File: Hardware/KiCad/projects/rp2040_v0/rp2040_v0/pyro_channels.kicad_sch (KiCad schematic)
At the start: 30 parts, among them J24 Screw_Terminal_01x02, J25 Screw_Terminal_01x02, J26 Screw_Terminal_01x02, J27 Screw_Terminal_01x02, J28 Screw_Terminal_01x02, Q2 AO3400A, Q3 AO3400A, Q4 AO3400A, Q5 AO3400A

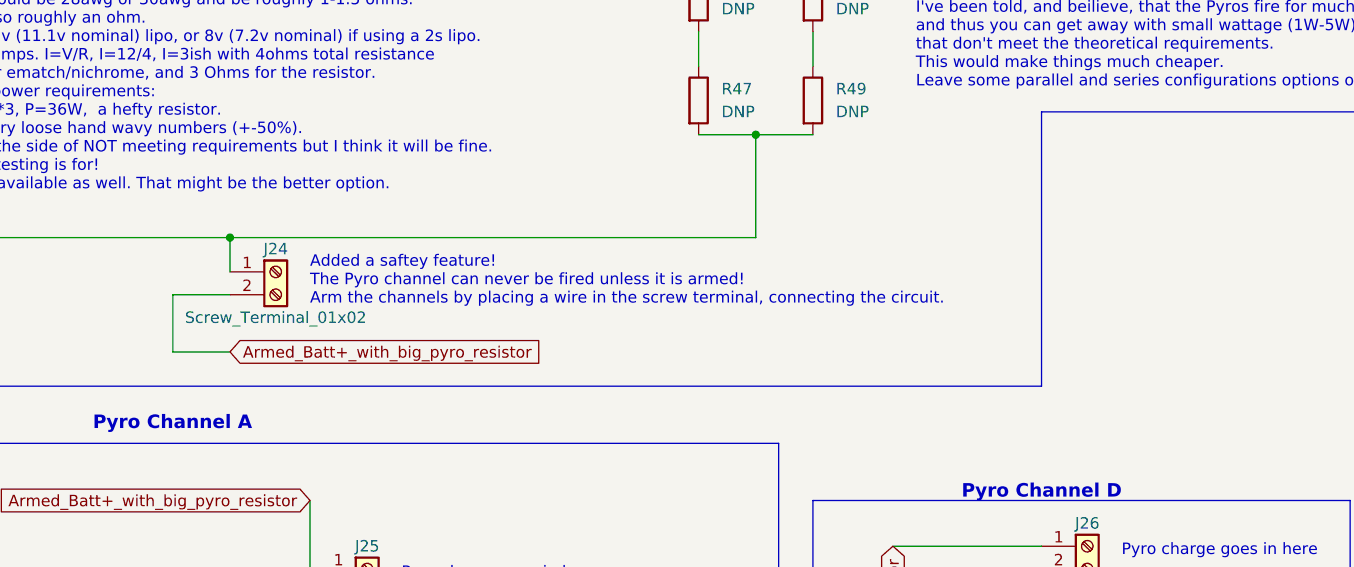
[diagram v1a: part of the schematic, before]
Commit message: Change arming screw terminal to jumper
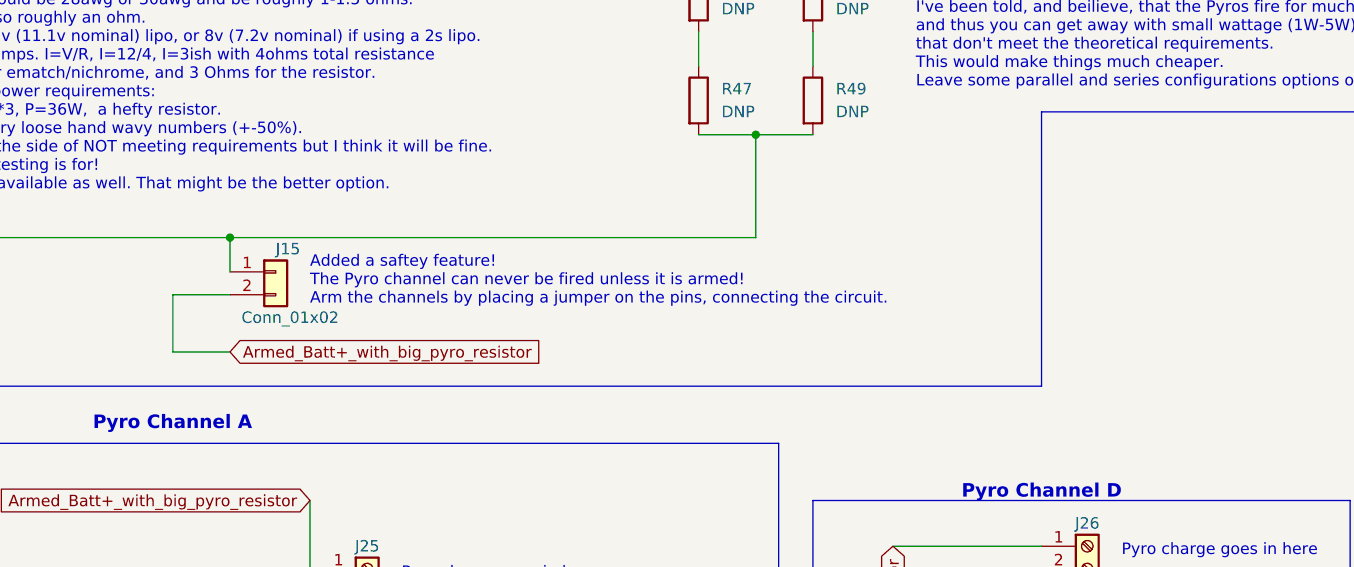
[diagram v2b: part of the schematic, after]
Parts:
- removed J24: Screw_Terminal_01x02, easyeda2kicad:CONN-TH_XY301V-A-5.0-2P, symbol Connector:Screw_Terminal_01x02
- added J15: Conn_01x02, Connector_PinHeader_2.54mm:PinHeader_1x02_P2.54mm_Vertical, symbol Connector_Generic:Conn_01x02
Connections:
- net Armed_Batt+_with_big_pyro_resistor: now also J15.2 (Pin_2)
- net at R39.2, R47.2, R49.2: now also J15.1 (Pin_1)
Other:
- note added: "Added a saftey feature! The Pyro channel can never be fired unless it is armed! Arm the channels by placing a jumper on the pins, connecting the circuit."
- note removed: "Added a saftey feature! The Pyro channel can never be fired unless it is armed! Arm the channels by placing a wire in the screw terminal, connecting the circuit."
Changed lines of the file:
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@@
     (effects (font (size 1.27 1.27)) (justify left bottom))
   )
-  (text "Added a saftey feature!\nThe Pyro channel can never be fired unless it is armed!\nArm the channels by placing a wire in the screw terminal, connecting the circuit."
+  (text "Added a saftey feature!\nThe Pyro channel can never be fired unless it is armed!\nArm the channels by placing a jumper on the pins, connecting the circuit."
     (at 83.82 76.2 0)
     (effects (font (size 1.27 1.27)) (justify left bottom))
@@
     (pin "1")
   )
+  (symbol (lib_id "Connector_Generic:Conn_01x02") (at 80.01 72.39 0) (unit 1)
+    (in_bom yes) (on_board yes)
+    (property "Reference" "J15" (id 0) (at 80.01 69.85 0)
+      (effects (font (size 1.27 1.27)) (justify left))
+    )
+    (property "Value" "Conn_01x02" (id 1) (at 76.2 77.47 0)
+      (effects (font (size 1.27 1.27)) (justify left))
+    )
+    (property "Footprint" "Connector_PinHeader_2.54mm:PinHeader_1x02_P2.54mm_Vertical" (id 2) (at 80.01 72.39 0)
+      (effects (font (size 1.27 1.27)) hide)
+    )
+    (property "Datasheet" "~" (id 3) (at 80.01 72.39 0)
+      (effects (font (size 1.27 1.27)) hide)
+    )
+    (pin "1")
+    (pin "2")
+  )
   (symbol (lib_id "Device:R_Small") (at 238.76 91.44 180) (unit 1)
     (in_bom yes) (on_board yes) (fields_autoplaced)
@@
     (pin "1")
   )
-  (symbol (lib_id "Connector:Screw_Terminal_01x02") (at 80.01 72.39 0) (unit 1)
-    (in_bom yes) (on_board yes)
-    (property "Reference" "J24" (id 0) (at 80.01 69.85 0))
-    (property "Value" "Screw_Terminal_01x02" (id 1) (at 80.01 77.47 0))
-    (property "Footprint" "easyeda2kicad:CONN-TH_XY301V-A-5.0-2P" (id 2) (at 80.01 72.39 0)
-      (effects (font (size 1.27 1.27)) hide)
-    )
-    (property "Datasheet" "~" (id 3) (at 80.01 72.39 0)
-      (effects (font (size 1.27 1.27)) hide)
-    )
-    (pin "1")
-    (pin "2")
-  )
   (symbol (lib_id "power:GND") (at 97.79 140.97 0) (unit 1)

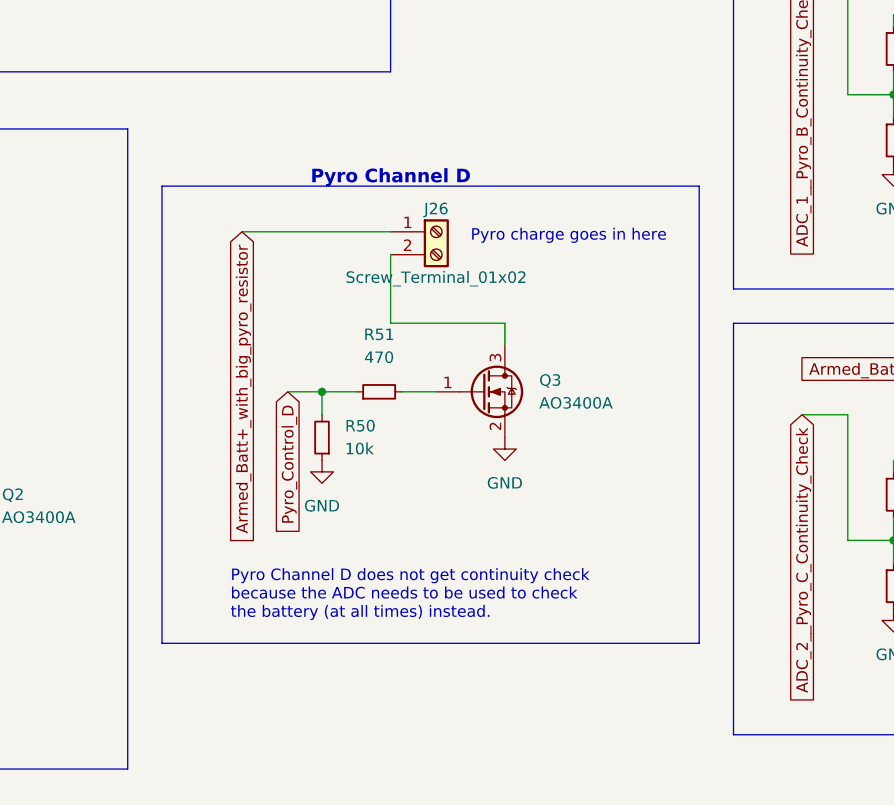
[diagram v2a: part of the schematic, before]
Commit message: Remove pyro channel D
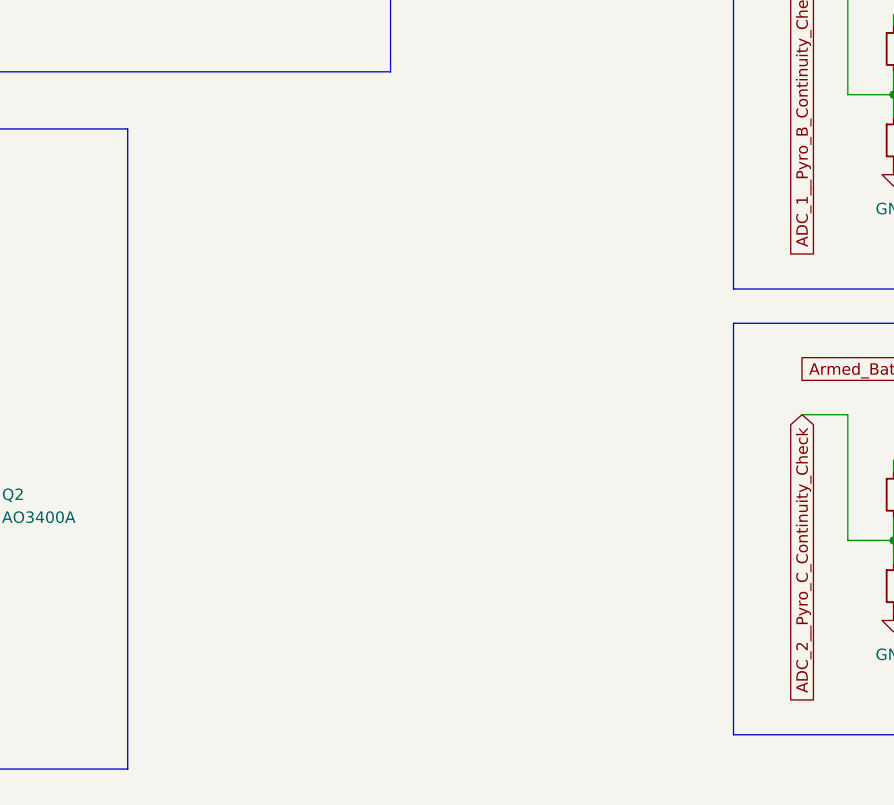
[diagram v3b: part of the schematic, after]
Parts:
- removed J26: Screw_Terminal_01x02, easyeda2kicad:CONN-TH_XY301V-A-5.0-2P, symbol Connector:Screw_Terminal_01x02
- removed Q3: AO3400A, Package_TO_SOT_SMD:SOT-23, symbol Transistor_FET:AO3400A
- removed R50: 10k, Resistor_SMD:R_0402_1005Metric, symbol Device:R_Small
- removed R51: 470, Resistor_SMD:R_0402_1005Metric, symbol Device:R_Small
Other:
- note removed: "Pyro Channel D"
- note removed: "Pyro Channel D does not get continuity check because the ADC needs to be used to check the battery (at all times) instead."
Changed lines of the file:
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@@
   (junction (at 246.38 78.74) (diameter 0) (color 0 0 0 0)
   )
-  (junction (at 157.48 120.65) (diameter 0) (color 0 0 0 0)
-  )
   (junction (at 31.75 27.94) (diameter 0) (color 0 0 0 0)
   )
@@
     (stroke (width 0) (type default) (color 0 0 0 0))
   )
-  (wire (pts (xy 177.8 115.57) (xy 177.8 113.03))
-    (stroke (width 0) (type default) (color 0 0 0 0))
-  )
   (wire (pts (xy 220.98 78.74) (xy 246.38 78.74))
     (stroke (width 0) (type default) (color 0 0 0 0))
@@
     (stroke (width 0) (type default) (color 0 0 0 0))
   )
-  (wire (pts (xy 157.48 120.65) (xy 161.29 120.65))
-    (stroke (width 0) (type default) (color 0 0 0 0))
-  )
   (wire (pts (xy 259.08 78.74) (xy 246.38 78.74))
     (stroke (width 0) (type default) (color 0 0 0 0))
@@
     (stroke (width 0) (type default) (color 0 0 0 0))
   )
-  (wire (pts (xy 165.1 105.41) (xy 165.1 113.03))
-    (stroke (width 0) (type default) (color 0 0 0 0))
-  )
   (wire (pts (xy 55.88 173.99) (xy 55.88 180.34))
     (stroke (width 0) (type default) (color 0 0 0 0))
@@
     (stroke (width 0) (type default) (color 0 0 0 0))
   )
-  (wire (pts (xy 177.8 113.03) (xy 165.1 113.03))
-    (stroke (width 0) (type default) (color 0 0 0 0))
-  )
   (polyline (pts (xy 203.2 158.75) (xy 284.48 158.75))
     (stroke (width 0) (type default) (color 0 0 0 0))
@@
     (stroke (width 0) (type default) (color 0 0 0 0))
   )
-  (wire (pts (xy 148.59 102.87) (xy 165.1 102.87))
-    (stroke (width 0) (type default) (color 0 0 0 0))
-  )
   (wire (pts (xy 127 57.15) (xy 133.35 57.15))
     (stroke (width 0) (type default) (color 0 0 0 0))
@@
     (stroke (width 0) (type default) (color 0 0 0 0))
   )
-  (wire (pts (xy 157.48 120.65) (xy 157.48 123.19))
-    (stroke (width 0) (type default) (color 0 0 0 0))
-  )
   (wire (pts (xy 215.9 137.16) (xy 220.98 137.16))
     (stroke (width 0) (type default) (color 0 0 0 0))
@@
     (stroke (width 0) (type default) (color 0 0 0 0))
   )
-  (polyline (pts (xy 199.39 97.79) (xy 139.7 97.79))
-    (stroke (width 0) (type default) (color 0 0 0 0))
-  )
   (wire (pts (xy 97.79 133.35) (xy 101.6 133.35))
     (stroke (width 0) (type default) (color 0 0 0 0))
@@
     (stroke (width 0) (type default) (color 0 0 0 0))
   )
-  (polyline (pts (xy 139.7 148.59) (xy 199.39 148.59))
-    (stroke (width 0) (type default) (color 0 0 0 0))
-  )
   (wire (pts (xy 133.35 57.15) (xy 133.35 68.58))
     (stroke (width 0) (type default) (color 0 0 0 0))
@@
     (stroke (width 0) (type default) (color 0 0 0 0))
   )
-  (wire (pts (xy 153.67 120.65) (xy 157.48 120.65))
-    (stroke (width 0) (type default) (color 0 0 0 0))
-  )
   (polyline (pts (xy 135.89 91.44) (xy 15.24 91.44))
     (stroke (width 0) (type default) (color 0 0 0 0))
@@
     (stroke (width 0) (type default) (color 0 0 0 0))
   )
-  (polyline (pts (xy 139.7 97.79) (xy 139.7 148.59))
-    (stroke (width 0) (type default) (color 0 0 0 0))
-  )
   (polyline (pts (xy 165.1 54.61) (xy 231.14 54.61))
     (stroke (width 0) (type default) (color 0 0 0 0))
@@
     (stroke (width 0) (type default) (color 0 0 0 0))
   )
-  (polyline (pts (xy 199.39 97.79) (xy 199.39 148.59))
-    (stroke (width 0) (type default) (color 0 0 0 0))
-  )
   (polyline (pts (xy 15.24 162.56) (xy 135.89 162.56))
     (stroke (width 0) (type default) (color 0 0 0 0))
@@
   )
   (wire (pts (xy 259.08 128.27) (xy 246.38 128.27))
-    (stroke (width 0) (type default) (color 0 0 0 0))
-  )
-  (wire (pts (xy 166.37 120.65) (xy 170.18 120.65))
     (stroke (width 0) (type default) (color 0 0 0 0))
   )
@@
     (effects (font (size 1.27 1.27)) (justify left bottom))
   )
-  (text "Pyro Channel D" (at 156.21 97.79 0)
-    (effects (font (size 1.5 1.5) (thickness 0.3) bold) (justify left bottom))
-  )
   (text "Inrush current\nprotection resistor" (at 95.25 125.73 0)
     (effects (font (size 1.27 1.27)) (justify left bottom))
@@
     (effects (font (size 1.5 1.5) (thickness 0.3) bold) (justify left bottom))
   )
-  (text "Pyro Channel D does not get continuity check\nbecause the ADC needs to be used to check\nthe battery (at all times) instead."
-    (at 147.32 146.05 0)
-    (effects (font (size 1.27 1.27)) (justify left bottom))
-  )
-  (text "Pyro charge goes in here" (at 173.99 104.14 0)
-    (effects (font (size 1.27 1.27)) (justify left bottom))
-  )
   (text "Pyro power source with resistor\n" (at 107.95 15.24 0)
     (effects (font (size 1.5 1.5) (thickness 0.3) bold) (justify left bottom))
@@
     )
   )
-  (global_label "Pyro_Control_D" (shape input) (at 153.67 120.65 270) (fields_autoplaced)
-    (effects (font (size 1.27 1.27)) (justify right))
-    (property "Intersheet References" "${INTERSHEET_REFS}" (id 0) (at 153.5906 129.4131 90)
-      (effects (font (size 1.27 1.27)) (justify right) hide)
-    )
-  )
   (global_label "ADC_1__Pyro_B_Continuity_Check" (shape input) (at 210.82 73.66 270) (fields_autoplaced)
     (effects (font (size 1.27 1.27)) (justify right))
@@
     (effects (font (size 1.27 1.27)) (justify right))
     (property "Intersheet References" "${INTERSHEET_REFS}" (id 0) (at 215.4221 118.1894 0)
-      (effects (font (size 1.27 1.27)) (justify right) hide)
-    )
-  )
-  (global_label "Armed_Batt+_with_big_pyro_resistor" (shape input) (at 148.59 102.87 270) (fields_autoplaced)
-    (effects (font (size 1.27 1.27)) (justify right))
-    (property "Intersheet References" "${INTERSHEET_REFS}" (id 0) (at 148.6694 132.5579 90)
       (effects (font (size 1.27 1.27)) (justify right) hide)
     )
@@
     )
   )
-  (symbol (lib_id "Device:R_Small") (at 163.83 120.65 90) (unit 1)
-    (in_bom yes) (on_board yes) (fields_autoplaced)
-    (property "Reference" "R51" (id 0) (at 163.83 114.3 90))
-    (property "Value" "470" (id 1) (at 163.83 116.84 90))
-    (property "Footprint" "Resistor_SMD:R_0402_1005Metric" (id 2) (at 163.83 120.65 0)
-      (effects (font (size 1.27 1.27)) hide)
-    )
-    (property "Datasheet" "~" (id 3) (at 163.83 120.65 0)
-      (effects (font (size 1.27 1.27)) hide)
-    )
-    (pin "1")
-    (pin "2")
-  )
   (symbol (lib_id "power:GND") (at 238.76 143.51 0) (unit 1)
     (in_bom yes) (on_board yes) (fields_autoplaced)
@@
     (pin "1")
   )
-  (symbol (lib_id "Device:R_Small") (at 157.48 125.73 180) (unit 1)
-    (in_bom yes) (on_board yes) (fields_autoplaced)
-    (property "Reference" "R50" (id 0) (at 160.02 124.4599 0)
-      (effects (font (size 1.27 1.27)) (justify right))
-    )
-    (property "Value" "10k" (id 1) (at 160.02 126.9999 0)
-      (effects (font (size 1.27 1.27)) (justify right))
-    )
-    (property "Footprint" "Resistor_SMD:R_0402_1005Metric" (id 2) (at 157.48 125.73 0)
-      (effects (font (size 1.27 1.27)) hide)
-    )
-    (property "Datasheet" "~" (id 3) (at 157.48 125.73 0)
-      (effects (font (size 1.27 1.27)) hide)
-    )
-    (pin "1")
-    (pin "2")
-  )
   (symbol (lib_id "Transistor_FET:AO3400A") (at 256.54 135.89 0) (unit 1)
     (in_bom yes) (on_board yes) (fields_autoplaced)
@@
     (pin "2")
     (pin "3")
-  )
-  (symbol (lib_id "power:GND") (at 157.48 128.27 0) (unit 1)
-    (in_bom yes) (on_board yes) (fields_autoplaced)
-    (property "Reference" "#PWR081" (id 0) (at 157.48 134.62 0)
-      (effects (font (size 1.27 1.27)) hide)
-    )
-    (property "Value" "GND" (id 1) (at 157.48 133.35 0))
-    (property "Footprint" "" (id 2) (at 157.48 128.27 0)
-      (effects (font (size 1.27 1.27)) hide)
-    )
-    (property "Datasheet" "" (id 3) (at 157.48 128.27 0)
-      (effects (font (size 1.27 1.27)) hide)
-    )
-    (pin "1")
   )
   (symbol (lib_id "power:GND") (at 259.08 140.97 0) (unit 1)
@@
     (pin "2")
   )
-  (symbol (lib_id "power:GND") (at 177.8 125.73 0) (unit 1)
-    (in_bom yes) (on_board yes) (fields_autoplaced)
-    (property "Reference" "#PWR082" (id 0) (at 177.8 132.08 0)
-      (effects (font (size 1.27 1.27)) hide)
-    )
-    (property "Value" "GND" (id 1) (at 177.8 130.81 0))
-    (property "Footprint" "" (id 2) (at 177.8 125.73 0)
-      (effects (font (size 1.27 1.27)) hide)
-    )
-    (property "Datasheet" "" (id 3) (at 177.8 125.73 0)
-      (effects (font (size 1.27 1.27)) hide)
-    )
-    (pin "1")
-  )
   (symbol (lib_id "power:+BATT") (at 22.86 27.94 90) (unit 1)
     (in_bom yes) (on_board yes)
@@
     (pin "2")
   )
-  (symbol (lib_id "Connector:Screw_Terminal_01x02") (at 170.18 102.87 0) (unit 1)
-    (in_bom yes) (on_board yes)
-    (property "Reference" "J26" (id 0) (at 170.18 100.33 0))
-    (property "Value" "Screw_Terminal_01x02" (id 1) (at 170.18 107.95 0))
-    (property "Footprint" "easyeda2kicad:CONN-TH_XY301V-A-5.0-2P" (id 2) (at 170.18 102.87 0)
-      (effects (font (size 1.27 1.27)) hide)
-    )
-    (property "Datasheet" "~" (id 3) (at 170.18 102.87 0)
-      (effects (font (size 1.27 1.27)) hide)
-    )
-    (pin "1")
-    (pin "2")
-  )
   (symbol (lib_id "power:GND") (at 259.08 91.44 0) (unit 1)
     (in_bom yes) (on_board yes) (fields_autoplaced)
@@
     (pin "1")
   )
-  (symbol (lib_id "Transistor_FET:AO3400A") (at 175.26 120.65 0) (unit 1)
-    (in_bom yes) (on_board yes) (fields_autoplaced)
-    (property "Reference" "Q3" (id 0) (at 181.61 119.3799 0)
-      (effects (font (size 1.27 1.27)) (justify left))
-    )
-    (property "Value" "AO3400A" (id 1) (at 181.61 121.9199 0)
-      (effects (font (size 1.27 1.27)) (justify left))
-    )
-    (property "Footprint" "Package_TO_SOT_SMD:SOT-23" (id 2) (at 180.34 122.555 0)
-      (effects (font (size 1.27 1.27) italic) (justify left) hide)
-    )
-    (property "Datasheet" "http://www.aosmd.com/pdfs/datasheet/AO3400A.pdf" (id 3) (at 175.26 120.65 0)
-      (effects (font (size 1.27 1.27)) (justify left) hide)
-    )
-    (pin "1")
-    (pin "2")
-    (pin "3")
-  )
   (symbol (lib_id "Device:R") (at 127 41.91 0) (unit 1)
